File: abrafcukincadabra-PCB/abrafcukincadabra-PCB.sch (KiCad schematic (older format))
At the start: 13 parts

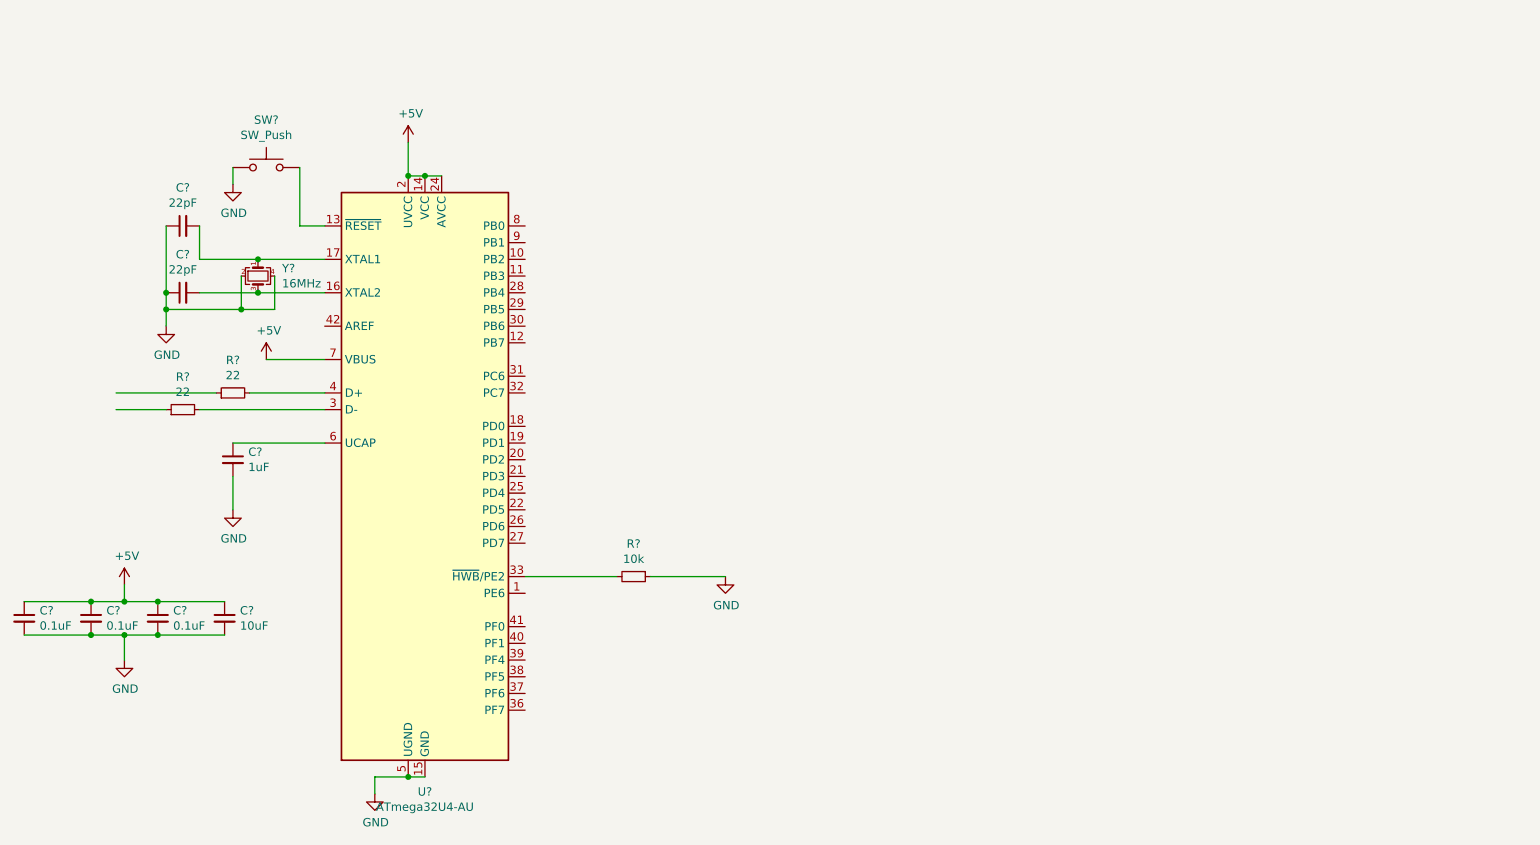
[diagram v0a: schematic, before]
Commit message: added autogenerated schematic
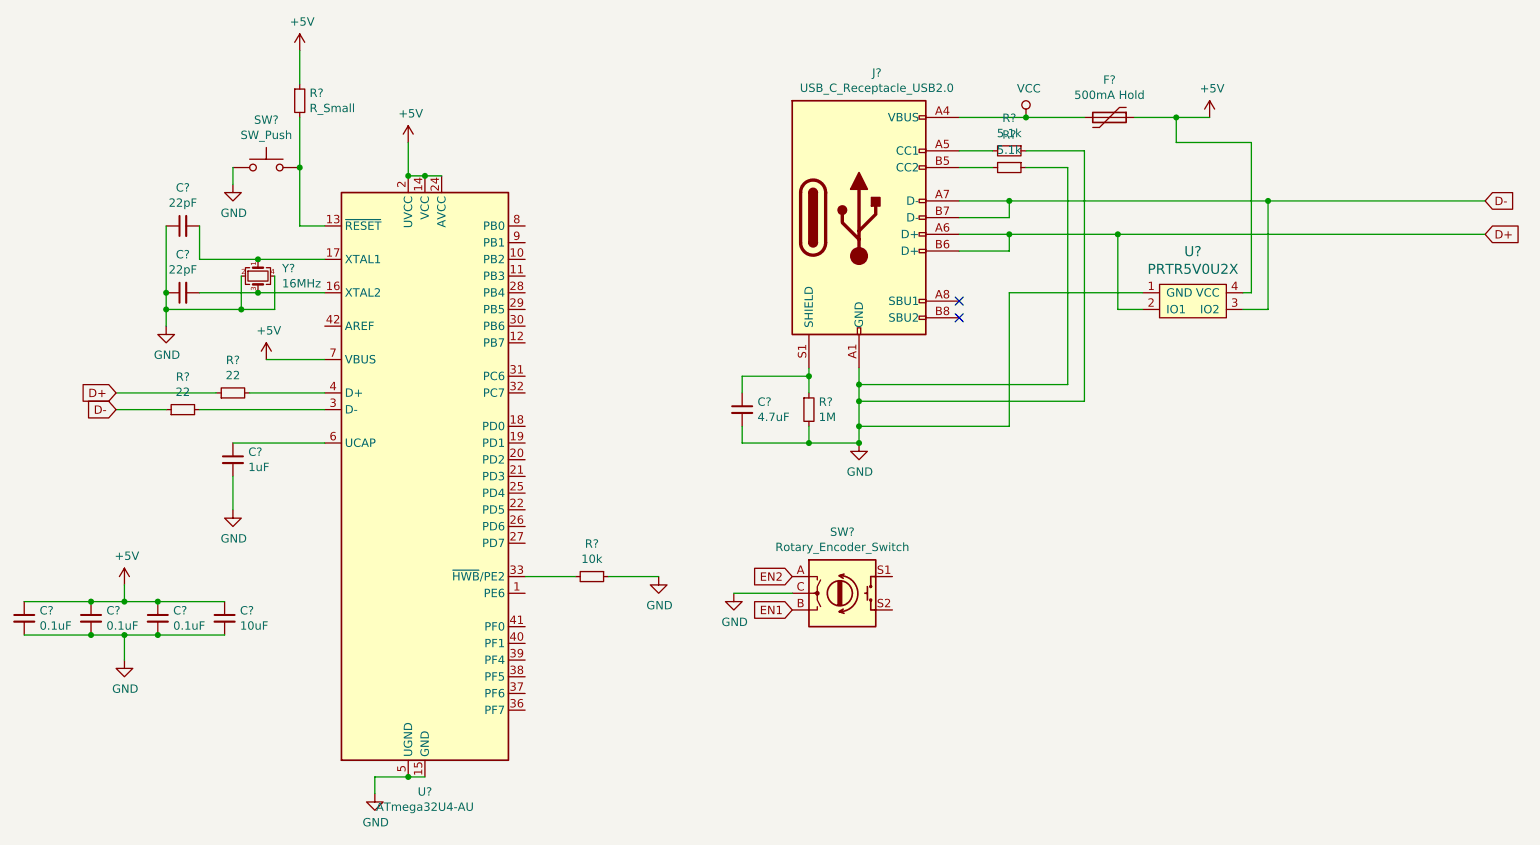
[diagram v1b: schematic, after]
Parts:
- added C?: 4.7uF, symbol Device:C_Small
- added F?: 500mA Hold, symbol Device:Polyfuse
- added J?: USB_C_Receptacle_USB2.0, symbol Connector:USB_C_Receptacle_USB2.0
- added R?: R_Small, symbol Device:R_Small
- added R?: 1M, symbol Device:R_Small
- added R? (x2): 5.1k, symbol Device:R_Small
- added SW?: Rotary_Encoder_Switch, symbol Device:Rotary_Encoder_Switch
- added U?: PRTR5V0U2X, symbol random-keyboard-parts:PRTR5V0U2X
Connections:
- net labels added: D+, D-, EN1, EN2, VCC
- wire segments 40 -> 88
- no-connect marks 0 -> 2
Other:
- moved on the sheet: R?
